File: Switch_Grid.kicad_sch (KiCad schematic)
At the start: 60 parts, among them K1 KEYSW, K10 KEYSW, K11 KEYSW, K12 KEYSW, K13 KEYSW, K14 KEYSW, K15 KEYSW, K16 KEYSW, K17 KEYSW, K18 KEYSW, K19 KEYSW, K2 KEYSW, K20 KEYSW, K21 KEYSW, K22 KEYSW, K23 KEYSW, K24 KEYSW, K25 KEYSW, K26 KEYSW, K27 KEYSW, K28 KEYSW, K29 KEYSW, K3 KEYSW, K30 KEYSW, K4 KEYSW, K5 KEYSW, K6 KEYSW, K7 KEYSW, K8 KEYSW, K9 KEYSW

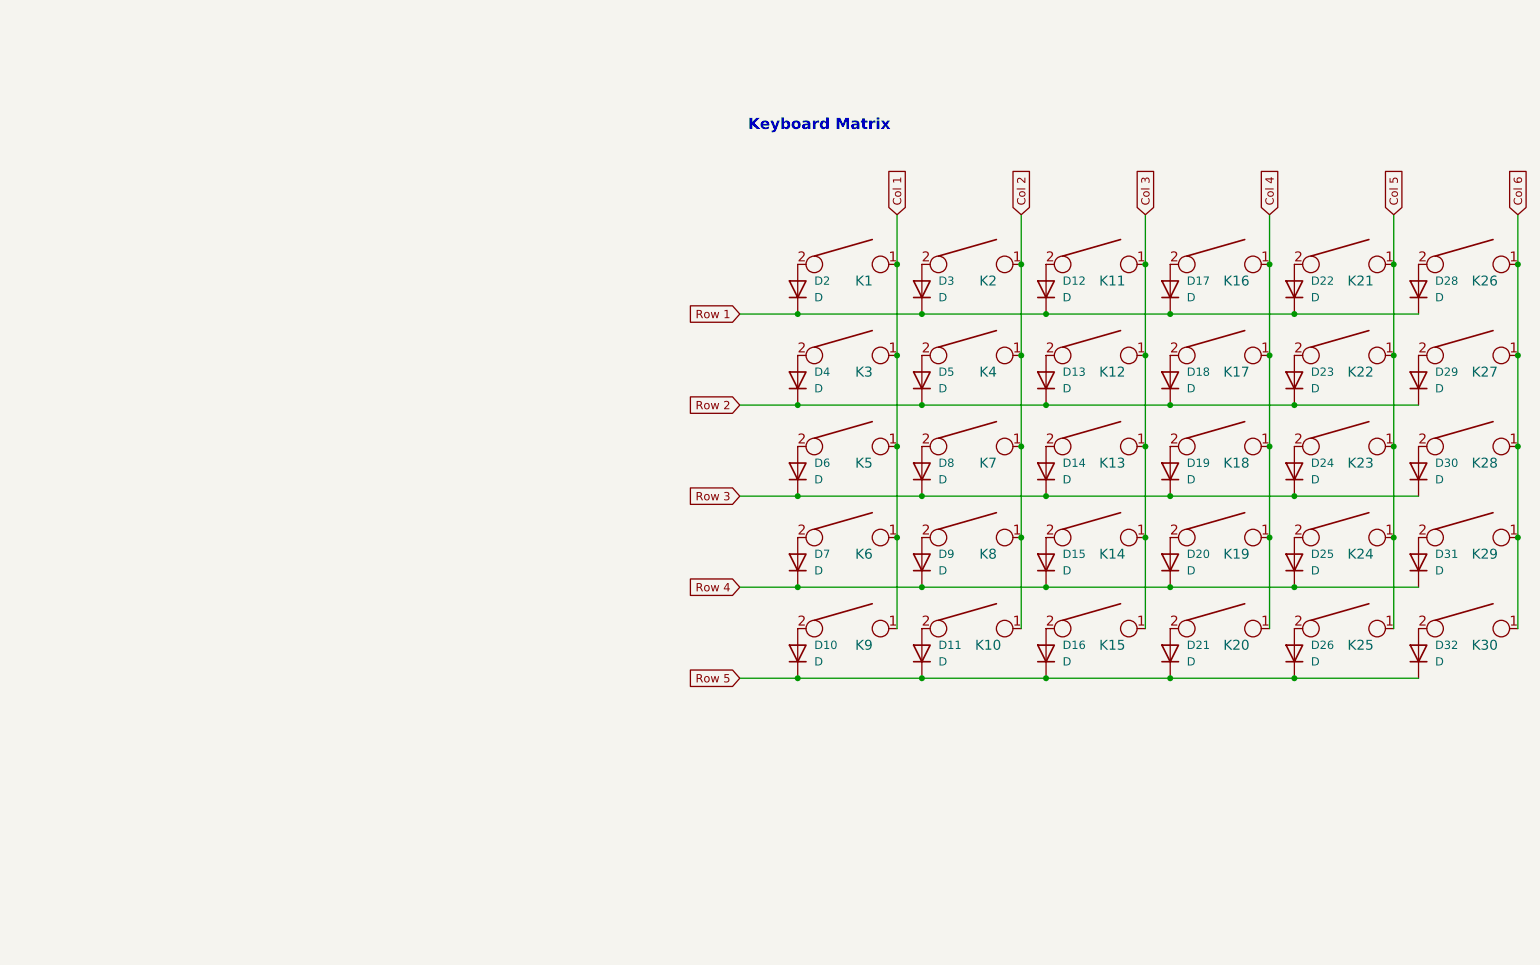
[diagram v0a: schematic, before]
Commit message: added mosfets for clearly marking what is powering board
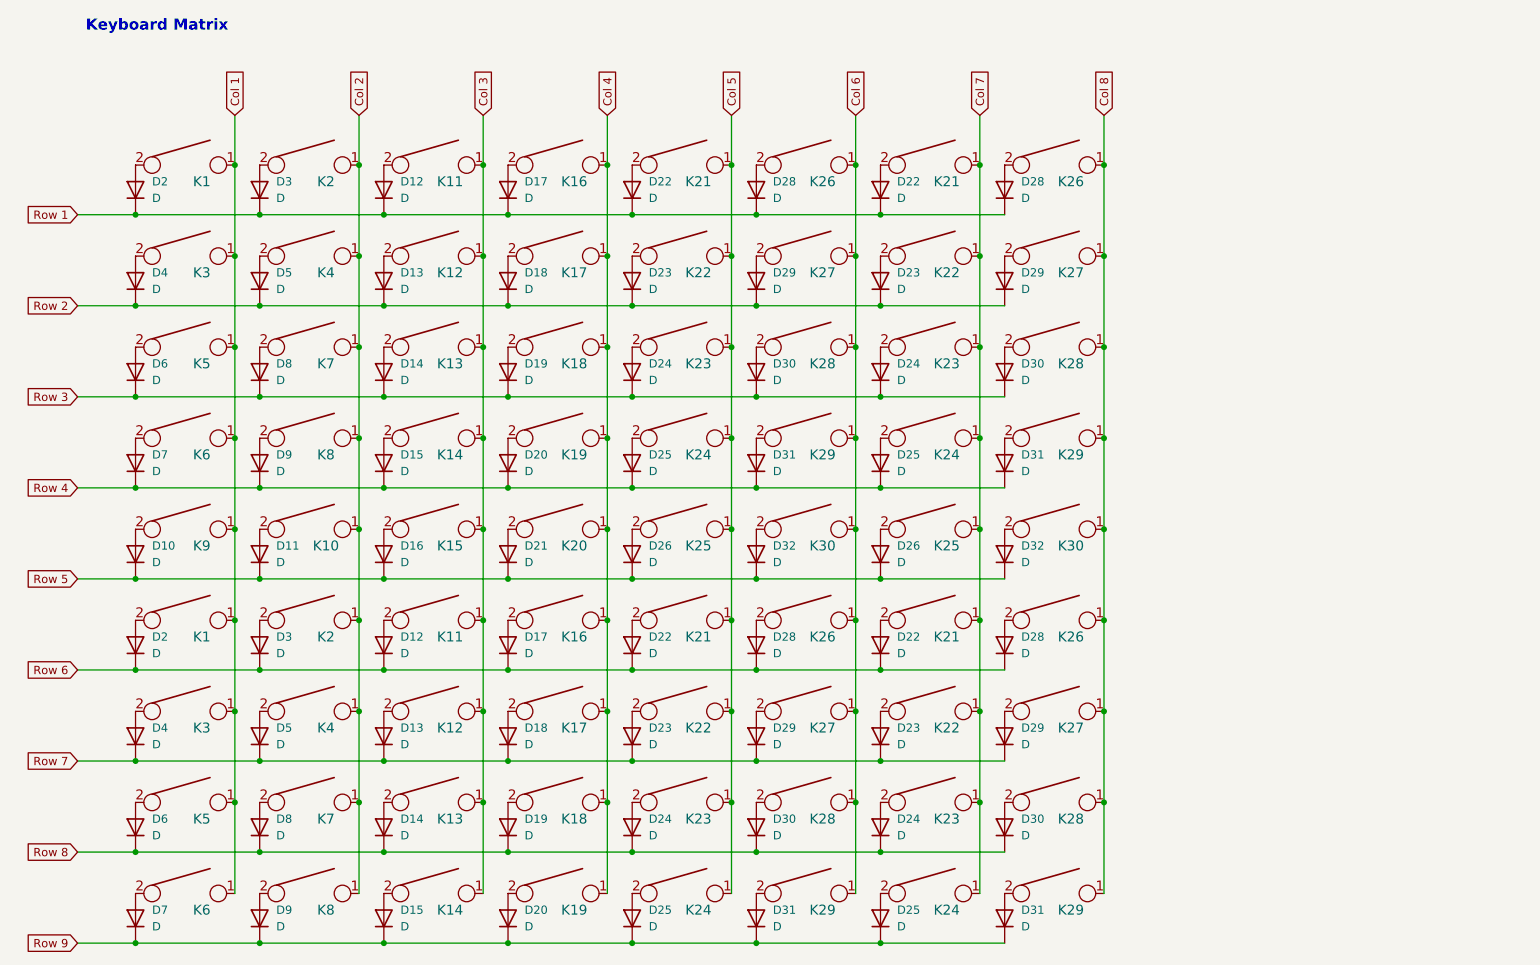
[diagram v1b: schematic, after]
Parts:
- added D12, D13, D14, D15, D17, D18, D19, D2, D20, D22 (x3), D23 (x3), D24 (x3), D25 (x3), D26, D28 (x3), D29 (x3), D3, D30 (x3), D31 (x3), D32, D4, D5, D6, D7, D8, D9: D, symbol Device:D
- added K1, K11, K12, K13, K14, K16, K17, K18, K19, K2, K21 (x3), K22 (x3), K23 (x3), K24 (x3), K25, K26 (x3), K27 (x3), K28 (x3), K29 (x3), K3, K30, K4, K5, K6, K7, K8: KEYSW, symbol keyboard_parts2:KEYSW
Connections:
- net Col 1: now also K1.1, K3.1, K5.1, K6.1
- net Col 2: now also K2.1, K4.1, K7.1, K8.1
- net Col 3: now also K11.1, K12.1, K13.1, K14.1
- net Col 4: now also K16.1, K17.1, K18.1, K19.1
- net Col 5: now also K21.1, K22.1, K23.1, K24.1
- net Col 6: now also K26.1, K27.1, K28.1, K29.1
- net Row 1: now also D22.1 (K), D28.1 (K)
- net Row 2: now also D23.1 (K), D29.1 (K)
- net Row 3: now also D24.1 (K), D30.1 (K)
- net Row 4: now also D25.1 (K), D31.1 (K)
- net Row 5: now also D26.1 (K), D32.1 (K)
- new net: D29.2 (A), K27.2 (x3)
- new net: D26.2 (A), K25.2
- new net: D12.2 (A), K11.2
- new net: D24.2 (A), K23.2 (x3)
- new net: D25.2 (A), K24.2 (x3)
- new net: D31.2 (A), K29.2 (x3)
- new net: D30.2 (A), K28.2 (x3)
- new net: D6.2 (A), K5.2
- new net: D4.2 (A), K3.2
- new net: D18.2 (A), K17.2
- new net: D17.2 (A), K16.2
- new net: D15.2 (A), K14.2
- new net: D22.2 (A), K21.2 (x3)
- new net: D28.2 (A), K26.2 (x3)
- new net: D19.2 (A), K18.2
- new net: D7.2 (A), K6.2
- new net: D23.2 (A), K22.2 (x3)
- new net: D5.2 (A), K4.2
- new net: D32.2 (A), K30.2
- new net: D9.2 (A), K8.2
- new net: D14.2 (A), K13.2
- new net: D2.2 (A), K1.2
- new net: D8.2 (A), K7.2
- new net: D20.2 (A), K19.2
- new net: D13.2 (A), K12.2
- new net: D3.2 (A), K2.2
- new net Col 7: K21.1, K21.1, K22.1, K22.1, K23.1, K23.1, K24.1, K24.1, K25.1
- new net Col 8: K26.1, K26.1, K27.1, K27.1, K28.1, K28.1, K29.1, K29.1, K30.1
- new net Row 6: D12.1 (K), D17.1 (K), D2.1 (K), D22.1 (K), D22.1 (K), D28.1 (K), D28.1 (K), D3.1 (K)
- new net Row 7: D13.1 (K), D18.1 (K), D23.1 (K), D23.1 (K), D29.1 (K), D29.1 (K), D4.1 (K), D5.1 (K)
- new net Row 8: D14.1 (K), D19.1 (K), D24.1 (K), D24.1 (K), D30.1 (K), D30.1 (K), D6.1 (K), D8.1 (K)
- new net Row 9: D15.1 (K), D20.1 (K), D25.1 (K), D25.1 (K), D31.1 (K), D31.1 (K), D7.1 (K), D9.1 (K)
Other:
- moved on the sheet: D10, D11, D12, D13, D14, D15, D16, D17, D18, D19, D2, D20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

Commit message: started on pcb
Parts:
- D10, D11, D12, D13, D14, D15, D16, D17, D18, D19, D2, D20, D21, D22, D23, D24, D25, D26, D28, D29, D3, D30, D31, D32, D4, D5, D6, D7, D8, D9: footprint (none) -> Diode_SMD:D_0603_1608Metric_Pad1.05x0.95mm_HandSolder
- K1, K10, K11, K12, K13, K14, K15, K16, K17, K18, K19, K2, K20, K21, K22, K23, K24, K25, K26, K27, K28, K29, K3, K30, K4, K5, K6, K7, K8, K9: footprint (none) -> Button_Switch_Keyboard:SW_Cherry_MX_1.00u_PCB
- K26: footprint (none) -> Button_Switch_Keyboard:SW_Cherry_MX_1.75u_PCB
- K28: footprint (none) -> Button_Switch_Keyboard:SW_Cherry_MX_2.00u_PCB

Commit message: finished logic layout, need to connect pins to keys
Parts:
- removed D11, D17, D19, D25, D28 (x2), D4, D8: D, Diode_SMD:D_0603_1608Metric_Pad1.05x0.95mm_HandSolder, symbol Device:D
- removed K10, K16, K18, K24, K26 (x2), K3, K7: KEYSW, Button_Switch_Keyboard:SW_Cherry_MX_1.00u_PCB, symbol keyboard_parts2:KEYSW
- K1: footprint Button_Switch_Keyboard:SW_Cherry_MX_1.00u_PCB -> Button_Switch_Keyboard:SW_Cherry_MX_6.25u_PCB
- K2, K29: footprint Button_Switch_Keyboard:SW_Cherry_MX_1.00u_PCB -> Button_Switch_Keyboard:SW_Cherry_MX_2.00u_PCB
- K23, K4: footprint Button_Switch_Keyboard:SW_Cherry_MX_1.00u_PCB -> Button_Switch_Keyboard:SW_Cherry_MX_1.25u_PCB
- K26: footprint Button_Switch_Keyboard:SW_Cherry_MX_1.75u_PCB -> Button_Switch_Keyboard:SW_Cherry_MX_1.50u_PCB
- K30: footprint Button_Switch_Keyboard:SW_Cherry_MX_1.00u_PCB -> Button_Switch_Keyboard:SW_Cherry_MX_1.50u_PCB
- K30: footprint Button_Switch_Keyboard:SW_Cherry_MX_1.00u_PCB -> Button_Switch_Keyboard:SW_Cherry_MX_2.25u_PCB
- K4: footprint Button_Switch_Keyboard:SW_Cherry_MX_1.00u_PCB -> Button_Switch_Keyboard:SW_Cherry_MX_1.75u_PCB
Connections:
- net Col 2: now also K14.1
- net Col 3: no longer K14.1
- net Col 4: now also K29.1
- net Col 6: now also K24.1; no longer K29.1
- net Col 7: no longer K24.1
- net Row 1: now also D25.1 (K), D31.1 (K)
- net Row 2: now also D7.1 (K)
- net Row 3: now also D31.1 (K)
- net Row 5: now also D9.1 (K)
- net Row 6: now also D20.1 (K)
- net Row 8: now also D15.1 (K)
- net Row 9: no longer D15.1 (K), D20.1 (K), D25.1 (K), D31.1 (K), D31.1 (K), D7.1 (K), D9.1 (K)
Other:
- moved on the sheet: D15, D20, D25, D31, D7, D9, K14, K19, K24, K29, K6, K8

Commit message: made further progress on the keyboard pcb
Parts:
- K1, K11, K12, K13, K14, K15, K16, K17, K18, K19, K2, K20, K21, K22, K23, K24, K25, K26, K27, K28, K29, K3, K5, K6, K7, K8, K9: footprint Button_Switch_Keyboard:SW_Cherry_MX_1.00u_PCB -> keyboard_parts:Cherry-MX_PCB-Mounted_LTST-A683CEGBW_Kailh_Socket
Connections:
- net Col 1: now also K2.1, K22.1, K27.1, K30.1, K30.1, K4.1, K4.1; no longer K1.1, K3.1, K5.1, K5.1, K6.1, K6.1, K9.1
- net Col 2: now also K15.1, K21.1, K23.1, K3.1, K5.1, K6.1; no longer K2.1, K2.1, K4.1, K4.1, K7.1, K8.1
- net Col 3: now also K17.1, K22.1, K23.1, K23.1, K29.1, K29.1; no longer K11.1, K12.1, K13.1, K13.1, K14.1, K15.1
- net Col 4: now also K1.1, K13.1, K21.1, K22.1, K25.1, K29.1; no longer K16.1, K17.1, K17.1, K18.1, K19.1, K29.1
- net Col 5: now also K21.1, K26.1, K27.1, K28.1, K28.1, K5.1, K7.1, K8.1; no longer K21.1, K21.1, K22.1, K22.1, K23.1, K23.1, K24.1, K25.1
- net Col 6: now also K11.1, K16.1, K17.1, K2.1, K27.1, K28.1, K6.1, K9.1; no longer K24.1, K26.1, K27.1, K27.1, K28.1, K28.1, K29.1, K30.1
- net Col 7: now also K12.1, K13.1, K14.1, K19.1, K24.1, K24.1, K26.1, K29.1; no longer K21.1, K21.1, K22.1, K22.1, K23.1, K23.1, K24.1, K25.1
- net Col 8: now also K18.1, K21.1, K22.1, K23.1, K24.1, K25.1, K27.1; no longer K26.1, K27.1, K27.1, K28.1, K29.1, K29.1, K30.1
- net Row 1: now also D18.1 (K), D2.1 (K), D20.1 (K), D26.1 (K), D29.1 (K), D6.1 (K), D9.1 (K); no longer D17.1 (K), D2.1 (K), D22.1 (K), D22.1 (K), D25.1 (K), D3.1 (K), D31.1 (K)
- net Row 2: now also D10.1 (K), D12.1 (K), D14.1 (K), D20.1 (K), D22.1 (K), D29.1 (K), D32.1 (K), D6.1 (K); no longer D13.1 (K), D18.1 (K), D23.1 (K), D23.1 (K), D29.1 (K), D29.1 (K), D5.1 (K), D7.1 (K)
- net Row 3: now also D13.1 (K), D16.1 (K), D23.1 (K), D25.1 (K), D28.1 (K), D5.1 (K), D7.1 (K); no longer D14.1 (K), D24.1 (K), D30.1 (K), D30.1 (K), D31.1 (K), D6.1 (K), D8.1 (K)
- net Row 4: now also D15.1 (K), D17.1 (K), D22.1 (K), D23.1 (K), D24.1 (K), D3.1 (K), D8.1 (K); no longer D15.1 (K), D20.1 (K), D25.1 (K), D31.1 (K), D31.1 (K), D7.1 (K), D9.1 (K)
- net Row 5: now also D18.1 (K), D2.1 (K), D24.1 (K), D24.1 (K), D31.1 (K), D5.1 (K), D9.1 (K); no longer D10.1 (K), D16.1 (K), D21.1 (K), D26.1 (K), D32.1 (K), D32.1 (K), D9.1 (K)
- net Row 6: now also D13.1 (K), D19.1 (K), D21.1 (K), D29.1 (K), D30.1 (K), D30.1 (K), D7.1 (K); no longer D12.1 (K), D2.1 (K), D20.1 (K), D22.1 (K), D22.1 (K), D28.1 (K), D3.1 (K)
- net Row 7: now also D15.1 (K), D23.1 (K), D23.1 (K), D3.1 (K), D30.1 (K), D31.1 (K), D31.1 (K); no longer D13.1 (K), D18.1 (K), D23.1 (K), D23.1 (K), D29.1 (K), D29.1 (K), D5.1 (K)
- net Row 8: now also D22.1 (K), D22.1 (K), D25.1 (K), D29.1 (K), D31.1 (K), D32.1 (K); no longer D15.1 (K), D19.1 (K), D24.1 (K), D24.1 (K), D30.1 (K), D6.1 (K)
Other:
- moved on the sheet: D10, D12, D13, D14, D15, D16, D17, D18, D19, D2, D20, D21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
